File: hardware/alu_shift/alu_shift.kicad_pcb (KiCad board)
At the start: 4 copper layers, 99 x 99 mm, 213 parts, among them J1 Conn_02x17_Odd_Even, Q1 IRLML6244, Q10 IRLML6244, Q11 IRLML6244, Q12 IRLML6244, Q13 IRLML6244, Q14 IRLML6244, Q15 IRLML6244, Q16 IRLML6244, Q17 IRLML6244, Q18 IRLML6244, Q19 IRLML6244, Q2 IRLML6244, Q20 IRLML6244, Q21 IRLML6244, Q22 IRLML6244, Q23 IRLML6244, Q24 IRLML6244, Q25 IRLML6244, Q26 IRLML6244, Q27 IRLML6244, Q28 IRLML6244, Q29 IRLML6244, Q3 IRLML6244, Q30 IRLML6244, Q31 IRLML6244, Q32 IRLML6244, Q33 IRLML6244, Q34 IRLML6244, Q35 IRLML6244, Q4 IRLML6244, Q5 IRLML6244, Q6 IRLML6244, Q7 IRLML6244, Q8 IRLML6244, Q9 IRLML6244, U1 74HC00, U10 74HC00, U11 74HC00, U12 74HC00, U13 74HC00, U14 74HC00, U15 74HC00, U16 74HC00, U17 74HC00, U18 74HC00, U19 74HC00, U2 74HC00, U20 74HC00, U21 74HC00, U22 74HC00, U23 74HC00, U24 74HC00, U25 74HC00, U26 74HC00, U27 74HC00, U28 74HC00, U29 74HC00, U3 74HC00, U30 74HC00, U31 74HC00, U32 74HC00, U33 74HC00, U34 74HC00, U35 74HC00, U36 74HC00, U37 74HC00, U38 74HC00, U39 74HC00, U4 74HC00, U40 74HC00, U41 74HC00, U42 74HC00, U43 74HC00, U44 74HC00, U45 74HC00, U46 74HC00, U47 74HC00, U48 74HC00, U49 74HC00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

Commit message: finished ALU Shift module, all ALU modules completed
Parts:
- added C12: 10uF, Capacitor_SMD:C_0603_1608Metric_Pad1.08x0.95mm_HandSolder, F.Cu at (87.3, 82.1)
- added C2: 10uF, Capacitor_SMD:C_0603_1608Metric_Pad1.08x0.95mm_HandSolder, F.Cu at (90.3, 82.1)
- added C3: 10uF, Capacitor_SMD:C_0603_1608Metric_Pad1.08x0.95mm_HandSolder, F.Cu at (88.8, 82.1)
- added H1: MountingHole_Pad, MountingHole:MountingHole_2.2mm_M2_Pad, F.Cu at (170.2, 137.1)
- added H2: MountingHole_Pad, MountingHole:MountingHole_2.2mm_M2_Pad, F.Cu at (81.6, 137.1)
- added H3: MountingHole_Pad, MountingHole:MountingHole_2.2mm_M2_Pad, F.Cu at (81.6, 48.5)
- added H4: MountingHole_Pad, MountingHole:MountingHole_2.2mm_M2_Pad, F.Cu at (170.2, 48.5)
- added TP1: TestPoint, TestPoint:TestPoint_Pad_D2.0mm, B.Cu at (106.8, 59.2)
- added TP10: TestPoint, TestPoint:TestPoint_Pad_D2.0mm, B.Cu at (115.9, 70.0)
- added TP11: TestPoint, TestPoint:TestPoint_Pad_D2.0mm, B.Cu at (125.1, 70.0)
- added TP12: TestPoint, TestPoint:TestPoint_Pad_D2.0mm, B.Cu at (134.2, 70.0)
- added TP13: TestPoint, TestPoint:TestPoint_Pad_D2.0mm, B.Cu at (143.3, 70.0)
- added TP14: TestPoint, TestPoint:TestPoint_Pad_D2.0mm, B.Cu at (152.5, 70.0)
- added TP15: TestPoint, TestPoint:TestPoint_Pad_D2.0mm, B.Cu at (161.6, 70.0)
- added TP16: TestPoint, TestPoint:TestPoint_Pad_D2.0mm, B.Cu at (170.8, 70.0)
- added TP17: TestPoint, TestPoint:TestPoint_Pad_D2.0mm, B.Cu at (106.8, 81.0)
- added TP18: TestPoint, TestPoint:TestPoint_Pad_D2.0mm, B.Cu at (115.9, 81.0)
- added TP19: TestPoint, TestPoint:TestPoint_Pad_D2.0mm, B.Cu at (125.1, 81.0)
- added TP2: TestPoint, TestPoint:TestPoint_Pad_D2.0mm, B.Cu at (115.9, 59.2)
- added TP20: TestPoint, TestPoint:TestPoint_Pad_D2.0mm, B.Cu at (134.2, 81.0)
- added TP21: TestPoint, TestPoint:TestPoint_Pad_D2.0mm, B.Cu at (143.3, 81.0)
- added TP22: TestPoint, TestPoint:TestPoint_Pad_D2.0mm, B.Cu at (152.5, 81.0)
- added TP23: TestPoint, TestPoint:TestPoint_Pad_D2.0mm, B.Cu at (161.6, 81.0)
- added TP24: TestPoint, TestPoint:TestPoint_Pad_D2.0mm, B.Cu at (170.8, 81.0)
- added TP25: TestPoint, TestPoint:TestPoint_Pad_D2.0mm, B.Cu at (106.8, 125.0)
- added TP26: TestPoint, TestPoint:TestPoint_Pad_D2.0mm, B.Cu at (115.9, 125.0)
- added TP27: TestPoint, TestPoint:TestPoint_Pad_D2.0mm, B.Cu at (125.1, 125.0)
- added TP28: TestPoint, TestPoint:TestPoint_Pad_D2.0mm, B.Cu at (134.2, 125.0)
- added TP29: TestPoint, TestPoint:TestPoint_Pad_D2.0mm, B.Cu at (143.3, 125.0)
- added TP3: TestPoint, TestPoint:TestPoint_Pad_D2.0mm, B.Cu at (125.1, 59.2)
- added TP30: TestPoint, TestPoint:TestPoint_Pad_D2.0mm, B.Cu at (152.5, 125.0)
- added TP31: TestPoint, TestPoint:TestPoint_Pad_D2.0mm, B.Cu at (161.6, 125.0)
- added TP32: TestPoint, TestPoint:TestPoint_Pad_D2.0mm, B.Cu at (170.8, 125.0)
- added TP33: TestPoint, TestPoint:TestPoint_Pad_D2.0mm, B.Cu at (106.8, 114.0)
- added TP34: TestPoint, TestPoint:TestPoint_Pad_D2.0mm, B.Cu at (115.9, 114.0)
- added TP35: TestPoint, TestPoint:TestPoint_Pad_D2.0mm, B.Cu at (125.1, 114.0)
- added TP36: TestPoint, TestPoint:TestPoint_Pad_D2.0mm, B.Cu at (134.2, 114.0)
- added TP37: TestPoint, TestPoint:TestPoint_Pad_D2.0mm, B.Cu at (143.3, 114.0)
- added TP38: TestPoint, TestPoint:TestPoint_Pad_D2.0mm, B.Cu at (152.5, 114.0)
- added TP39: TestPoint, TestPoint:TestPoint_Pad_D2.0mm, B.Cu at (161.6, 114.0)
- added TP4: TestPoint, TestPoint:TestPoint_Pad_D2.0mm, B.Cu at (134.2, 59.2)
- added TP40: TestPoint, TestPoint:TestPoint_Pad_D2.0mm, B.Cu at (170.8, 114.0)
- added TP41: TestPoint, TestPoint:TestPoint_Pad_D2.0mm, B.Cu at (106.8, 102.8)
- added TP42: TestPoint, TestPoint:TestPoint_Pad_D2.0mm, B.Cu at (115.9, 102.8)
- added TP43: TestPoint, TestPoint:TestPoint_Pad_D2.0mm, B.Cu at (125.1, 102.8)
- added TP44: TestPoint, TestPoint:TestPoint_Pad_D2.0mm, B.Cu at (134.2, 102.8)
- added TP45: TestPoint, TestPoint:TestPoint_Pad_D2.0mm, B.Cu at (143.3, 102.8)
- added TP46: TestPoint, TestPoint:TestPoint_Pad_D2.0mm, B.Cu at (152.5, 102.8)
- added TP47: TestPoint, TestPoint:TestPoint_Pad_D2.0mm, B.Cu at (161.6, 102.8)
- added TP48: TestPoint, TestPoint:TestPoint_Pad_D2.0mm, B.Cu at (170.8, 102.8)
- added TP49: TestPoint, TestPoint:TestPoint_Pad_D2.0mm, B.Cu at (94.0, 128.4)
- added TP5: TestPoint, TestPoint:TestPoint_Pad_D2.0mm, B.Cu at (143.3, 59.2)
- added TP50: TestPoint, TestPoint:TestPoint_Pad_D2.0mm, B.Cu at (94.0, 122.0)
- added TP6: TestPoint, TestPoint:TestPoint_Pad_D2.0mm, B.Cu at (152.5, 59.2)
- added TP7: TestPoint, TestPoint:TestPoint_Pad_D2.0mm, B.Cu at (161.6, 59.2)
- added TP8: TestPoint, TestPoint:TestPoint_Pad_D2.0mm, B.Cu at (170.8, 59.2)
- added TP9: TestPoint, TestPoint:TestPoint_Pad_D2.0mm, B.Cu at (106.8, 70.0)
- moved U1 320.8 mm to (86.9, 125.1), turned to 180 degrees
- moved C1 293.7 mm to (86.9, 130.5)
- moved D11 285.0 mm to (101.1, 48.7), turned to 180 degrees
- moved D9 280.5 mm to (119.3, 136.7)
- moved Q9 275.1 mm to (119.3, 133.8), turned to 90 degrees
- moved Q11 273.3 mm to (101.1, 51.6), turned to -90 degrees
- moved R11 271.9 mm to (101.1, 47.2), turned to 180 degrees
- moved R9 268.5 mm to (119.3, 138.2)
- moved Q10 203.0 mm to (114.3, 51.6), turned to -90 degrees
- moved Q12 203.0 mm to (117.8, 51.6), turned to -90 degrees
- moved Q13 203.0 mm to (121.3, 51.6), turned to -90 degrees
- moved D10 202.8 mm to (114.3, 48.7), turned to 180 degrees
- moved D12 202.8 mm to (117.8, 48.7), turned to 180 degrees
- moved D13 202.8 mm to (121.3, 48.7), turned to 180 degrees
- moved R10 202.8 mm to (114.3, 47.2), turned to 180 degrees
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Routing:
- net +5V: track 746.5 -> 989.1 mm, vias 63 -> 65
- net /A7: track 0.00 -> 161.9 mm, vias 0 -> 5
- net /A0: track 0.00 -> 144.0 mm, vias 0 -> 5
- net /RES7: track 0.00 -> 121.8 mm, vias 0 -> 3
- net /A5: track 0.00 -> 117.9 mm, vias 0 -> 3
- net /A6: track 0.00 -> 117.2 mm, vias 0 -> 3
- net /A3: track 0.00 -> 113.9 mm, vias 0 -> 3
- net /A4: track 0.00 -> 112.8 mm, vias 0 -> 3
- net /RES6: track 0.00 -> 112.7 mm, vias 0 -> 3
- net /A1: track 0.00 -> 111.3 mm, vias 0 -> 3
- net /RES5: track 0.00 -> 109.7 mm, vias 0 -> 3
- net /A2: track 0.00 -> 109.3 mm, vias 0 -> 3
- net /RES4: track 0.00 -> 100.8 mm, vias 0 -> 3
- net /MuxResult/SEL: track 0.00 -> 100.6 mm, vias 0 -> 4
- net /RES3: track 0.00 -> 98.0 mm, vias 0 -> 3
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- added copper zone on F.Cu, net +5V
- removed copper zone on F.Cu, net GND
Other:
- board text added: "8 Bit Bidirectional Shifter Rev A"
- board text added: "A0"
- board text added: "A1"
- board text added: "A2"
- board text added: "A3"
- board text added: "A4"
- board text added: "A5"
- board text added: "A6"
- board text added: "A7"
- board text added: "BY"
- board text added: "BY0"
- board text added: "BY1"
- board text added: "BY2"
- board text added: "DIR"
- board text added: "GND"
- board text added: "IN"
- board text added: "RES"
- board text added: "RES0"
- board text added: "RES1"
- board text added: "RES2"
- board text added: "RES3"
- board text added: "RES4"
- board text added: "RES5"
- board text added: "RES6"
- board text added: "RES7"
- board text added: "SOB"
- board text added: "VCC"
- board text added: "mrab"

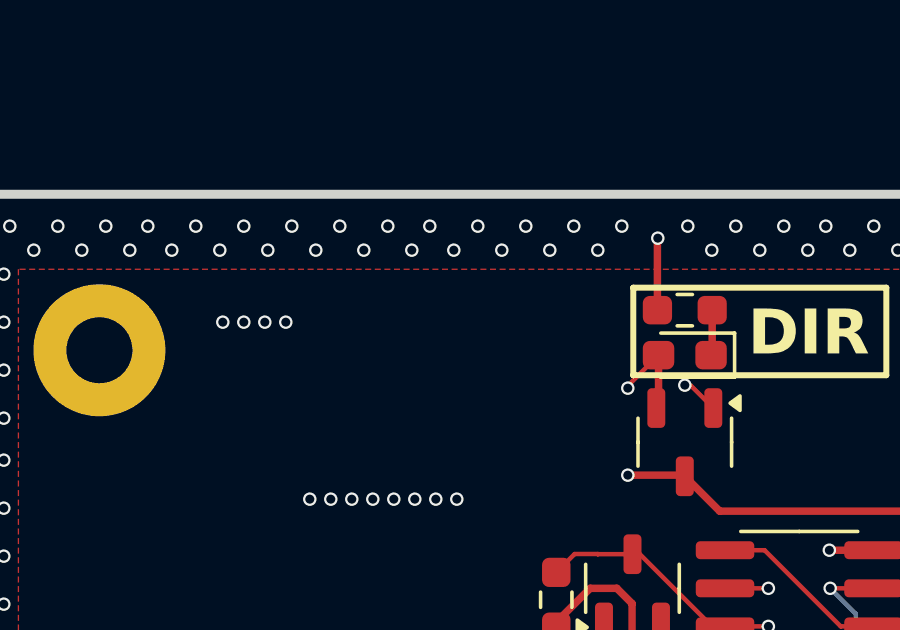
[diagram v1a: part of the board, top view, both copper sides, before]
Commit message: added PWR indicator to alu_shift
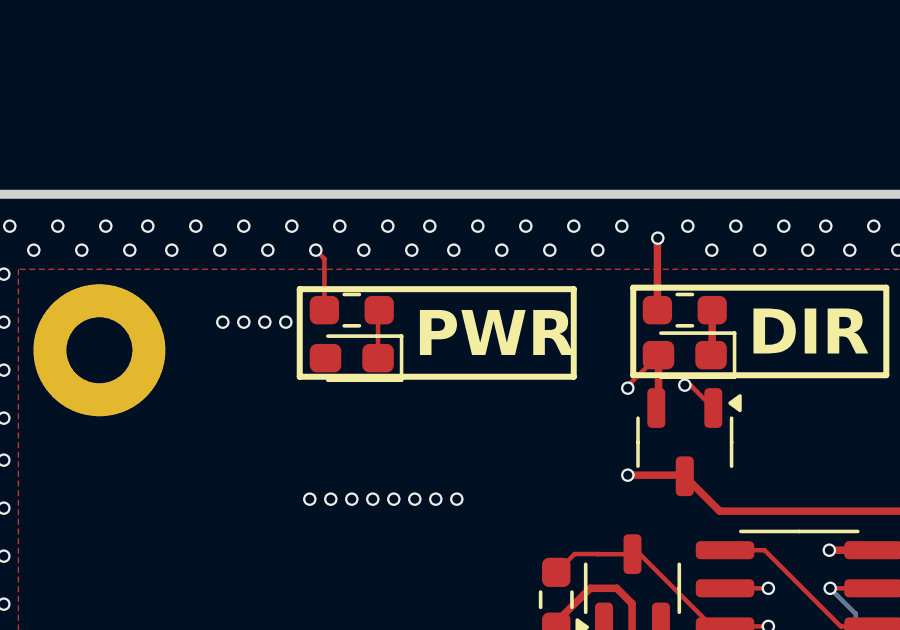
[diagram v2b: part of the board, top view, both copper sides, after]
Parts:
- added D22: LED, LED_SMD:LED_0603_1608Metric_Pad1.05x0.95mm_HandSolder, F.Cu at (90.0, 48.8)
- added R43: 1000, Resistor_SMD:R_0603_1608Metric_Pad0.98x0.95mm_HandSolder, F.Cu at (90.0, 47.2)
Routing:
- net GND: track 404.8 -> 406.9 mm
- net Net-(D22-K): track 0.00 -> 1.62 mm
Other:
- board text added: "PWR"

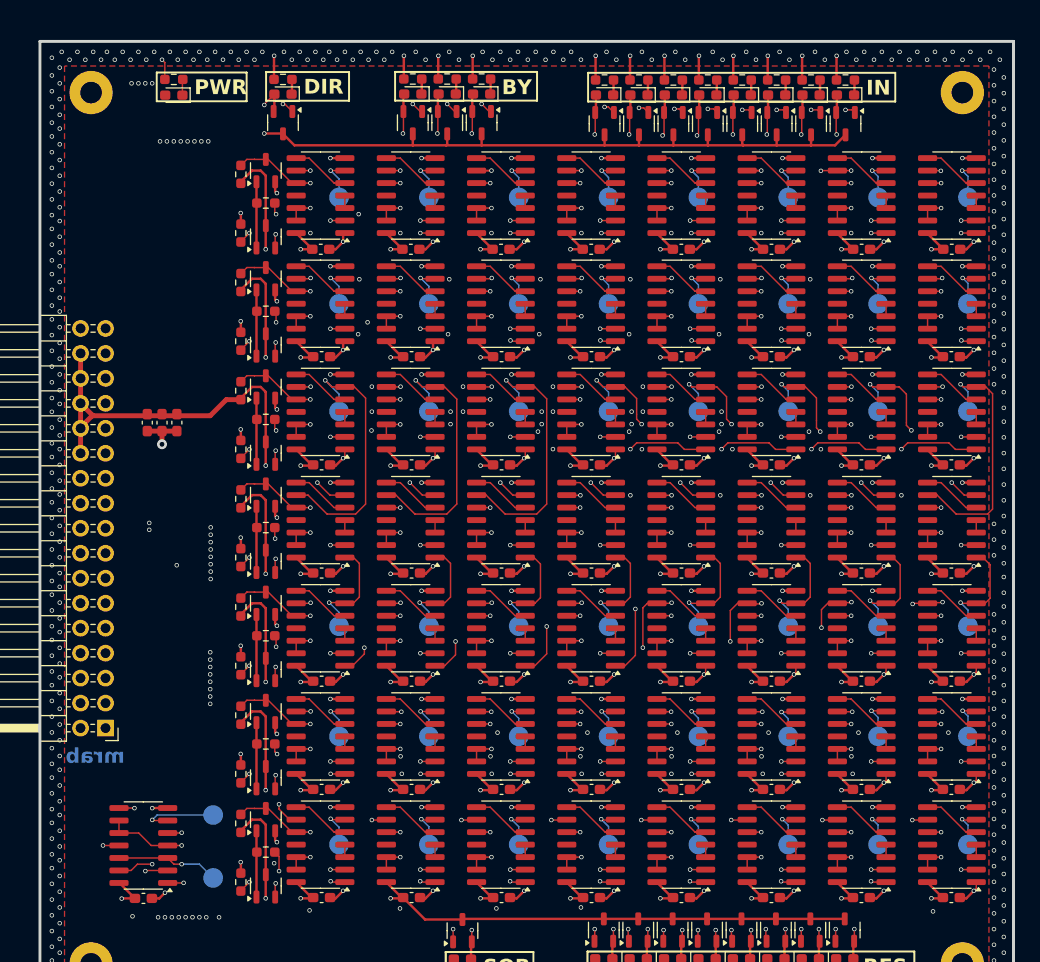
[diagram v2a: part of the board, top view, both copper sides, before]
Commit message: ALU shifter, bitops and motherboard as ordered
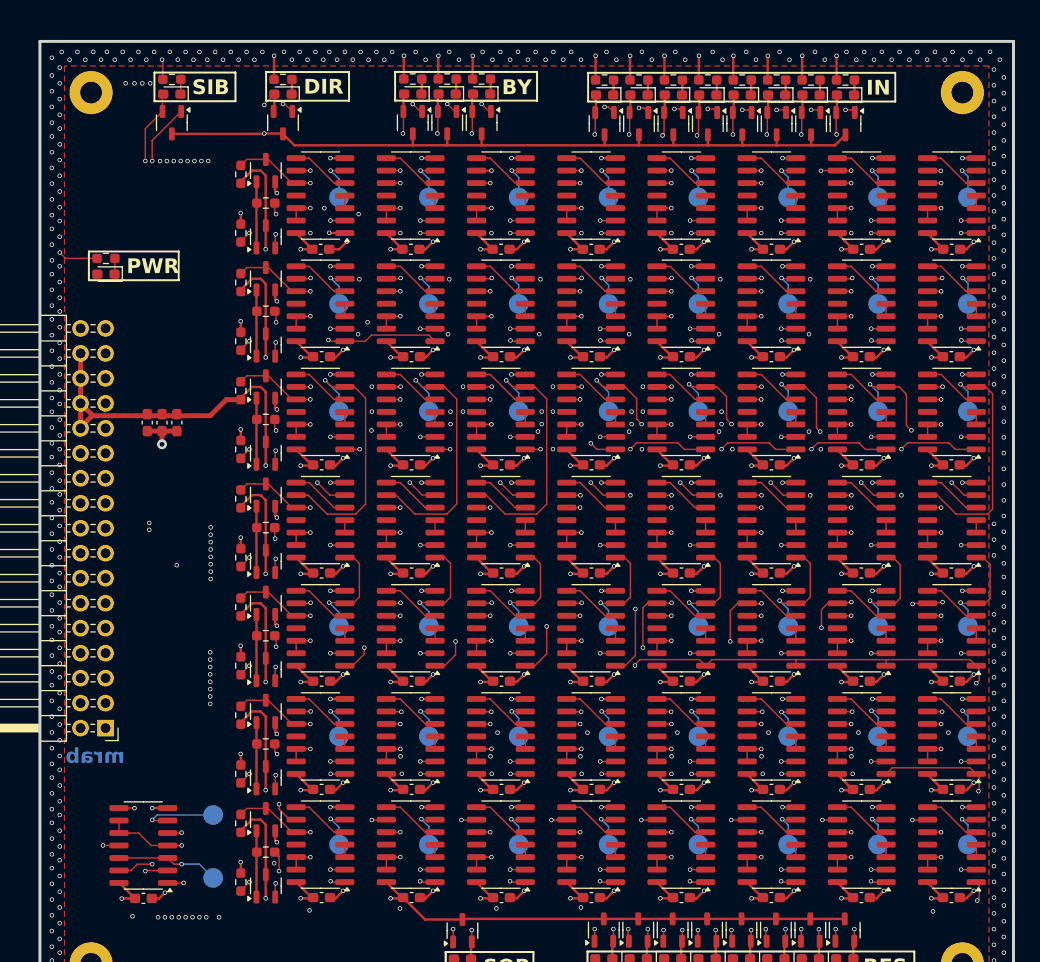
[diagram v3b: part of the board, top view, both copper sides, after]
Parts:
- added D23: LED, LED_SMD:LED_0603_1608Metric_Pad1.05x0.95mm_HandSolder, F.Cu at (89.8, 48.7)
- added Q36: IRLML6244, Package_TO_SOT_SMD:SOT-23-3, F.Cu at (89.8, 51.6)
- added R44: 1000, Resistor_SMD:R_0603_1608Metric_Pad0.98x0.95mm_HandSolder, F.Cu at (89.8, 47.2)
- moved D22 19.5 mm to (83.1, 67.0)
- moved R43 19.5 mm to (83.1, 65.4)
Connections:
- J1 pad 24: +5V -> /SIB
- U17 pad 1: GND -> /MuxLeft1/B0
- U2 pad 1: GND -> /MuxLeft1/B0
- U24 pad 1: GND -> /MuxLeft1/B0
- U25 pad 1: GND -> /MuxLeft1/B0
- U30 pad 1: GND -> /MuxLeft1/B0
- U31 pad 1: GND -> /MuxLeft1/B0
- U32 pad 1: GND -> /MuxLeft1/B0
- U33 pad 1: GND -> /MuxLeft1/B0
- U42 pad 1: GND -> /MuxLeft1/B0
- U43 pad 1: GND -> /MuxLeft1/B0
- U44 pad 1: GND -> /MuxLeft1/B0
- U45 pad 1: GND -> /MuxLeft1/B0
- U50 pad 1: GND -> /MuxLeft1/B0
- U51 pad 1: GND -> /MuxLeft1/B0
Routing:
- net /MuxLeft1/B0: track 0.00 -> 198.6 mm, vias 0 -> 12
- net /SIB: track 0.00 -> 40.1 mm, vias 0 -> 1
- net GND: track 406.9 -> 397.7 mm
- net +5V: track 989.1 -> 996.0 mm
- net Net-(D23-K): track 0.00 -> 1.52 mm
- net /BY2: track 67.3 -> 68.1 mm
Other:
- board text added: "SIB"
